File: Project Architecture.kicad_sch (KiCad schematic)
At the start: 0 parts

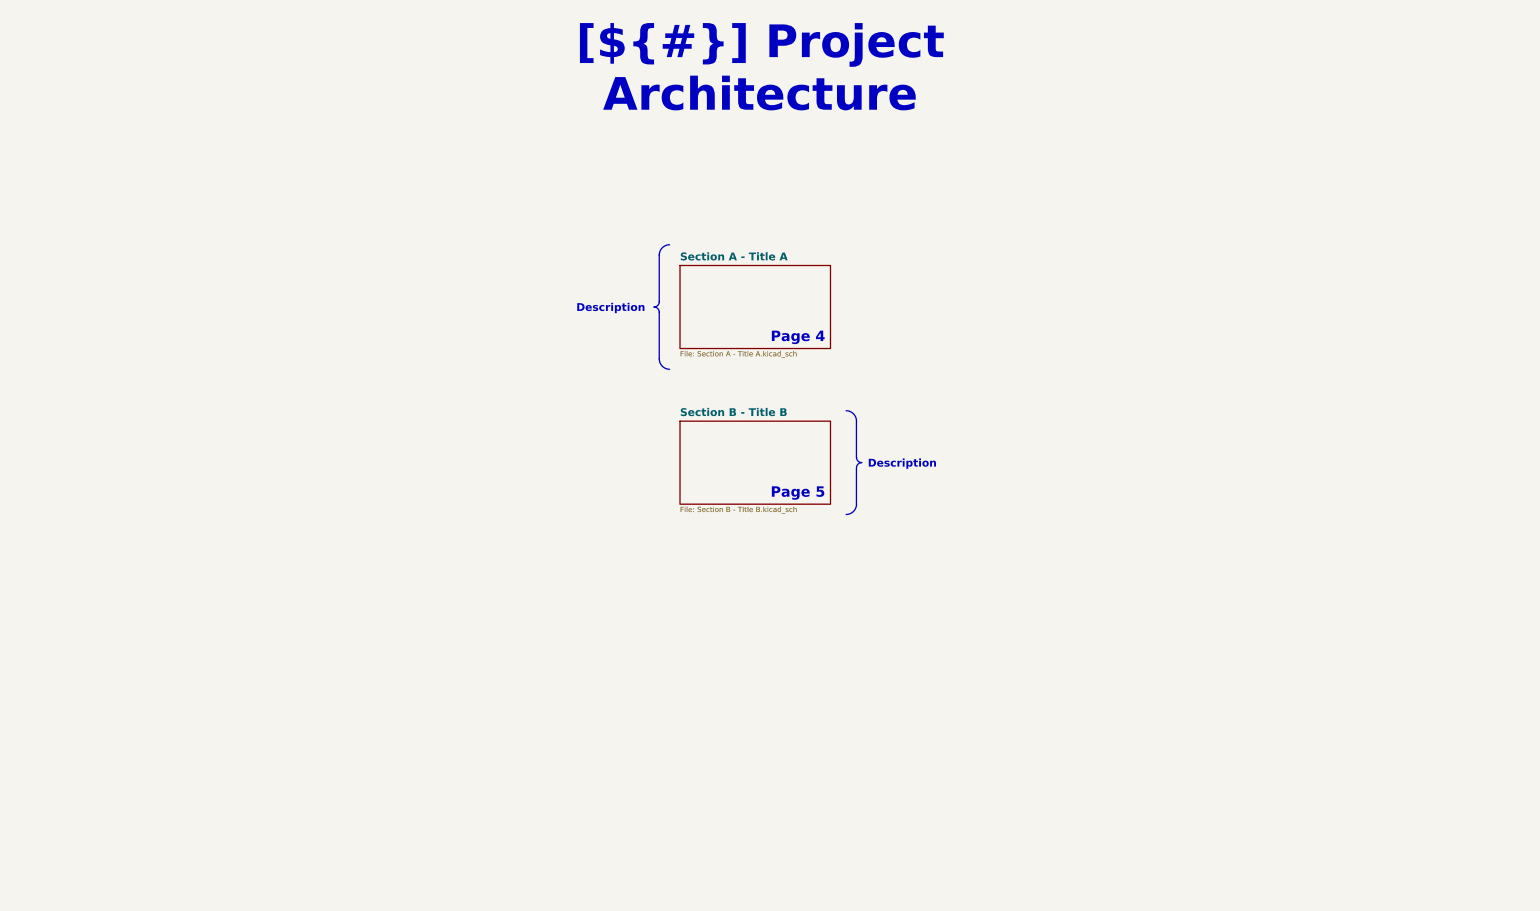
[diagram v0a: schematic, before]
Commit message: Save KiCad 10 design work
Snapshot of the schematic and PCB work done since the initial template
commit: AD7606C-18 ADC, 3x INA241A2 + PBV 1 mOhm shunts, MR60PW phase
connectors, LT8362 boost and LT3045-1 / LTC6655 analog supplies, project
libraries (lib/) and their sym/fp-lib-table.

.gitignore now excludes local history, SpinRender working files, the
stray .step export and Component Search Engine download leftovers.

Co-Authored-By: Claude Opus 5.5 <noreply@anthropic.com>
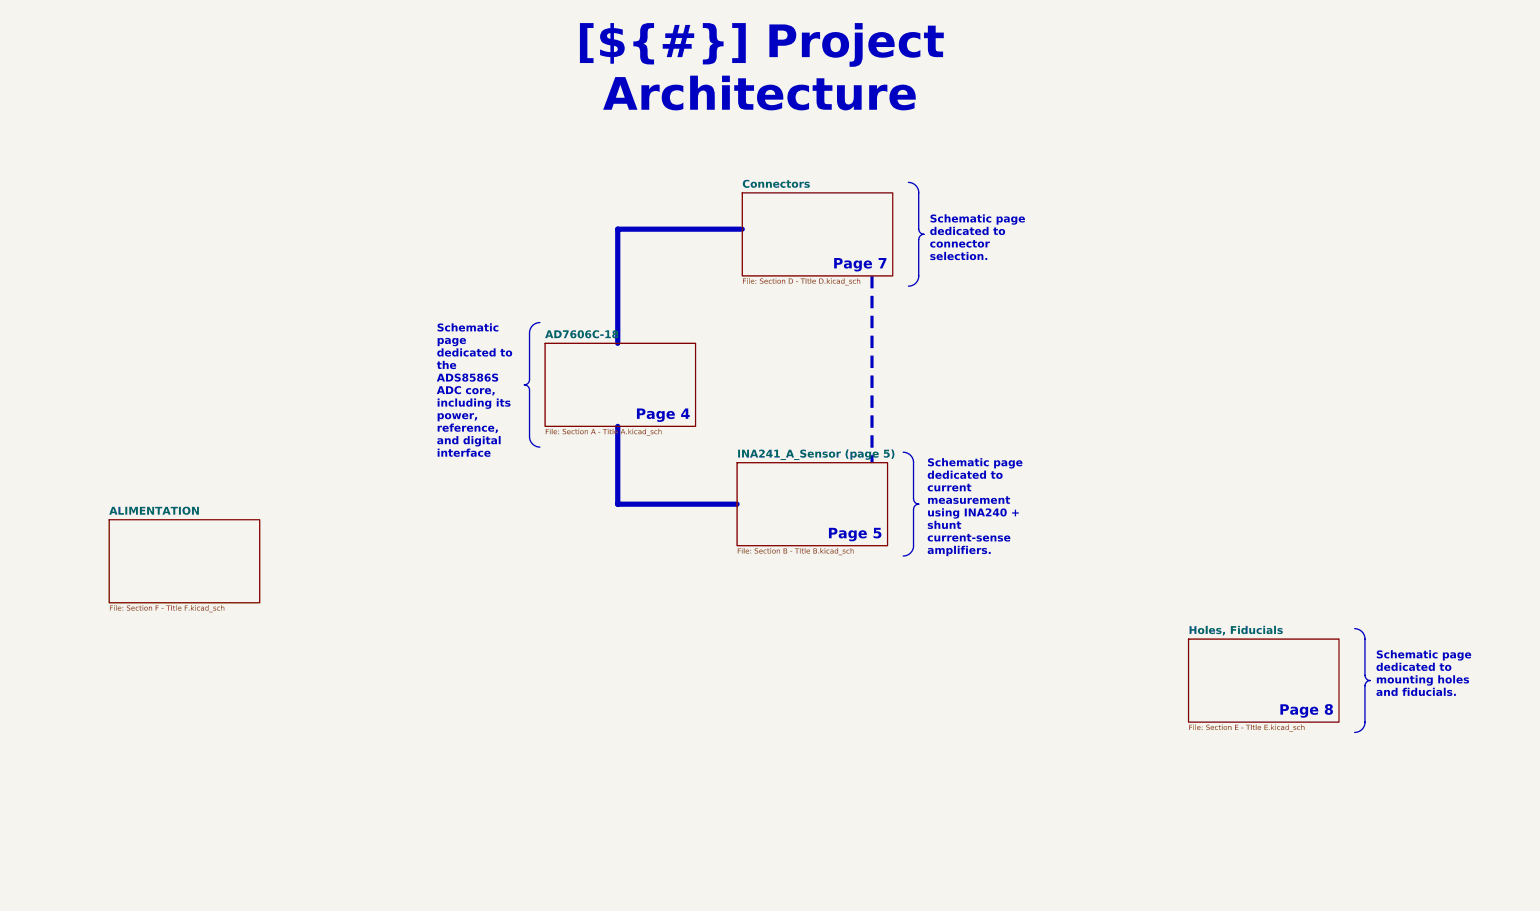
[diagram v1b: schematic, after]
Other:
- sheet Section A - Title A renamed AD7606C-18
- sheet Section B - Title B renamed INA241_A_Sensor (page 5)
- added sheet ALIMENTATION (Section F - TItle F.kicad_sch)
- added sheet Connectors (Section D - TItle D.kicad_sch)
- added sheet Holes, Fiducials (Section E - TItle E.kicad_sch)
- note added: "Page 7"
- note added: "Page 8"

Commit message: Rename to PhaseSense-8586, name sheets by function, self-contained library
Project and sheets
- INA240.* renamed PhaseSense-8586.* (the amplifier is an INA241 and the
  project name was already PhaseSense-8586 in kibot_main.yaml); symbol and
  sheet instances follow the new project name
- "Section X - Title X" sheets renamed after their function: AD7606C-18 -
  ADC, INA241 - Phase Current and Voltage Sense, Connectors, Holes -
  Fiducials, Power Supply - Boost 6V and Analog Rails; hierarchical net
  names updated in the PCB (schematic parity unchanged)
- real titles and dates in the title blocks; Project Architecture and gain
  notes now describe the fitted parts (AD7606C-18, INA241A2 = 20 V/V)

Libraries
- every symbol, footprint and 3D model used by the board is now in
  lib/lib_sym/PhaseSense-8586.kicad_sym, lib/lib_fp/PhaseSense-8586.pretty
  and lib/3d_models, referenced through ${KIPRJMOD}
- removes the footprints without library nickname, the absolute and
  bare-filename 3D paths and the modified-symbol copies (C_1, LT3045_1)

Connectivity is unchanged: the exported netlist is identical before and
after. ERC goes from 62 to 43 violations (footprint links and library
mismatches gone), DRC schematic parity from 33 to 20.

Co-Authored-By: Claude Opus 5.5 <noreply@anthropic.com>
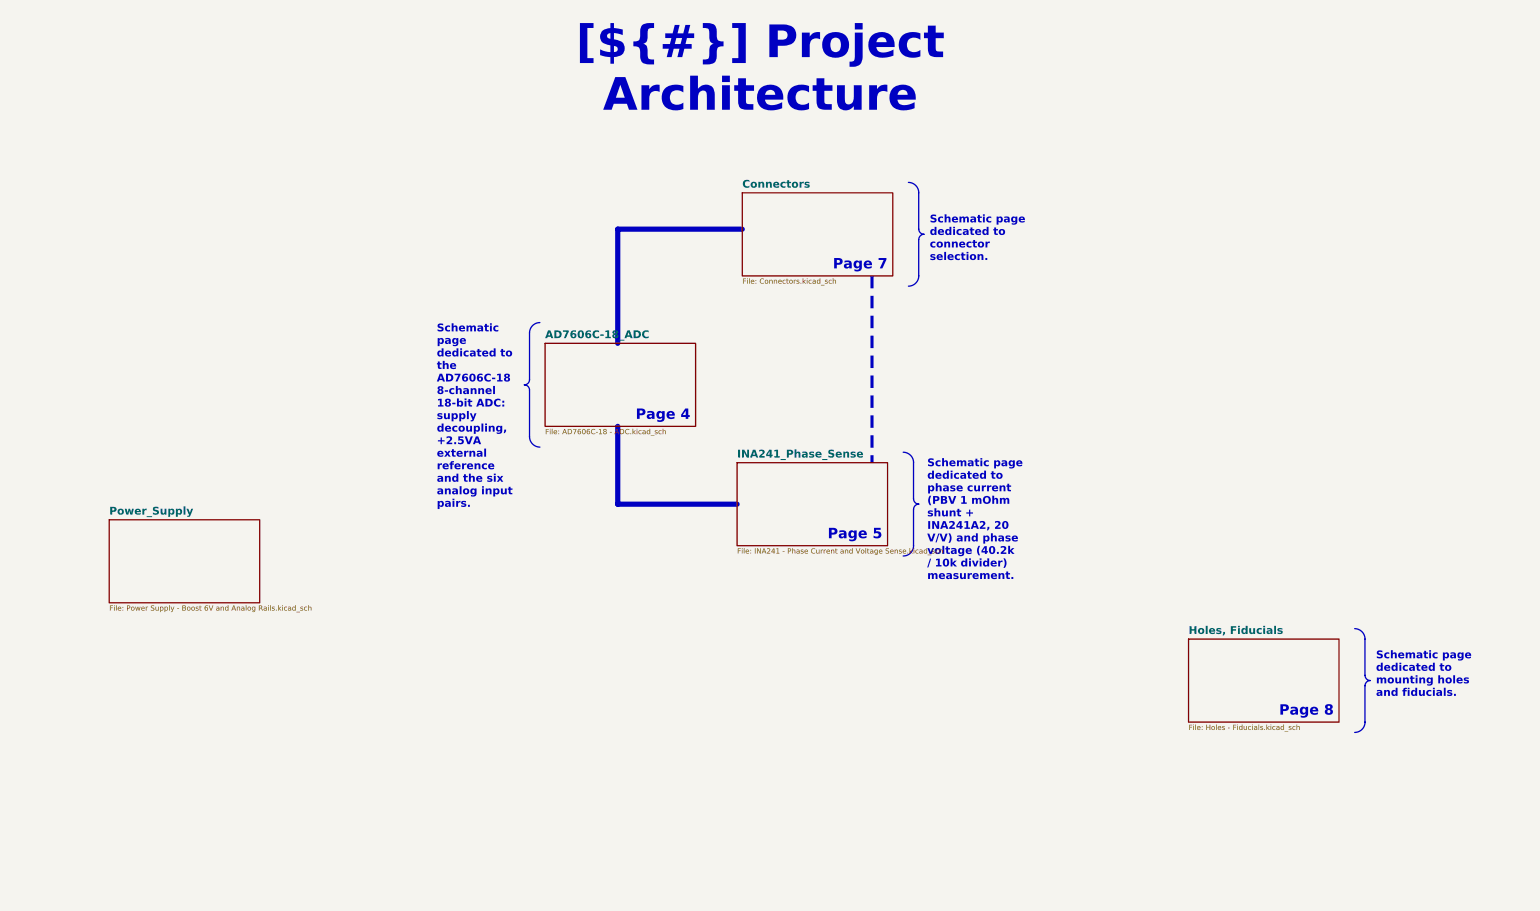
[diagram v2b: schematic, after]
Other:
- sheet AD7606C-18 renamed AD7606C-18_ADC
- sheet ALIMENTATION renamed Power_Supply
- sheet INA241_A_Sensor (page 5) renamed INA241_Phase_Sense
- sheet AD7606C-18_ADC: file Section A - Title A.kicad_sch -> AD7606C-18 - ADC.kicad_sch
- sheet Connectors: file Section D - TItle D.kicad_sch -> Connectors.kicad_sch
- sheet Holes, Fiducials: file Section E - TItle E.kicad_sch -> Holes - Fiducials.kicad_sch
- sheet INA241_Phase_Sense: file Section B - TItle B.kicad_sch -> INA241 - Phase Current and Voltage Sense.kicad_sch
- sheet Power_Supply: file Section F - TItle F.kicad_sch -> Power Supply - Boost 6V and Analog Rails.kicad_sch
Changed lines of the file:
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@@
 	(title_block
 		(title "Project Architecture")
-		(date "2025-01-12")
+		(date "2026-10-05")
 		(rev "${REVISION}")
 		(company "${COMPANY}")
@@
 		)
 	)
-	(text_box "Schematic page dedicated to the ADS8586S ADC core, including its power, reference, and digital interface"
+	(text_box "Schematic page dedicated to the AD7606C-18 8-channel 18-bit ADC: supply decoupling, +2.5VA external reference and the six analog input pairs."
 		(exclude_from_sim no)
 		(at 129.54 88.9 0)
@@
 		)
 	)
-	(text_box "Schematic page dedicated to current measurement using INA240 + shunt current-sense amplifiers."
+	(text_box "Schematic page dedicated to phase current (PBV 1 mOhm shunt + INA241A2, 20 V/V) and phase voltage (40.2k / 10k divider) measurement."
 		(exclude_from_sim no)
 		(at 249.575 121.9 0)
@@
 			(color 255 200 0 0.502)
 		)
-		(property "Sheetname" "ALIMENTATION"
+		(property "Sheetname" "Power_Supply"
 			(at 50.8 137.4009 0)
 			(show_name no)
@@
 			)
 		)
-		(property "Sheetfile" "Section F - TItle F.kicad_sch"
+		(property "Sheetfile" "Power Supply - Boost 6V and Analog Rails.kicad_sch"
 			(at 50.8 159.3346 0)
 			(show_name no)
@@
 		)
 		(instances
-			(project "INA240"
+			(project "PhaseSense-8586"
 				(path "/f9e05184-c88b-4a88-ae9c-ab2bdb32be7c/c5103ceb-5325-4a84-a025-9638a412984e"
 					(page "11")
@@
 			)
 		)
-		(property "Sheetfile" "Section E - TItle E.kicad_sch"
+		(property "Sheetfile" "Holes - Fiducials.kicad_sch"
 			(at 314.96 188.5446 0)
 			(show_name no)
@@
 		)
 		(instances
-			(project "INA240"
+			(project "PhaseSense-8586"
 				(path "/f9e05184-c88b-4a88-ae9c-ab2bdb32be7c/c5103ceb-5325-4a84-a025-9638a412984e"
 					(page "8")
@@
 			)
 		)
-		(property "Sheetfile" "Section D - TItle D.kicad_sch"
+		(property "Sheetfile" "Connectors.kicad_sch"
 			(at 205.74 79.3246 0)
 			(show_name no)
@@
 		)
 		(instances
-			(project "INA240"
+			(project "PhaseSense-8586"
 				(path "/f9e05184-c88b-4a88-ae9c-ab2bdb32be7c/c5103ceb-5325-4a84-a025-9638a412984e"
 					(page "7")
@@
 			(color 255 200 0 0.502)
 		)
-		(property "Sheetname" "INA241_A_Sensor (page 5)"
+		(property "Sheetname" "INA241_Phase_Sense"
 			(at 204.47 123.4309 0)
 			(show_name no)
@@
 			)
 		)
-		(property "Sheetfile" "Section B - TItle B.kicad_sch"
+		(property "Sheetfile" "INA241 - Phase Current and Voltage Sense.kicad_sch"
 			(at 204.47 145.3646 0)
 			(show_name no)
@@
 		)
 		(instances
-			(project "INA240"
+			(project "PhaseSense-8586"
 				(path "/f9e05184-c88b-4a88-ae9c-ab2bdb32be7c/c5103ceb-5325-4a84-a025-9638a412984e"
 					(page "5")
@@
 			(color 128 255 128 0.5)
 		)
-		(property "Sheetname" "AD7606C-18"
+		(property "Sheetname" "AD7606C-18_ADC"
 			(at 157.48 94.2209 0)
 			(show_name no)
@@
 			)
 		)
-		(property "Sheetfile" "Section A - Title A.kicad_sch"
+		(property "Sheetfile" "AD7606C-18 - ADC.kicad_sch"
 			(at 157.48 116.1546 0)
 			(show_name no)
@@
 		)
 		(instances
-			(project "INA240"
+			(project "PhaseSense-8586"
 				(path "/f9e05184-c88b-4a88-ae9c-ab2bdb32be7c/c5103ceb-5325-4a84-a025-9638a412984e"
 					(page "4")

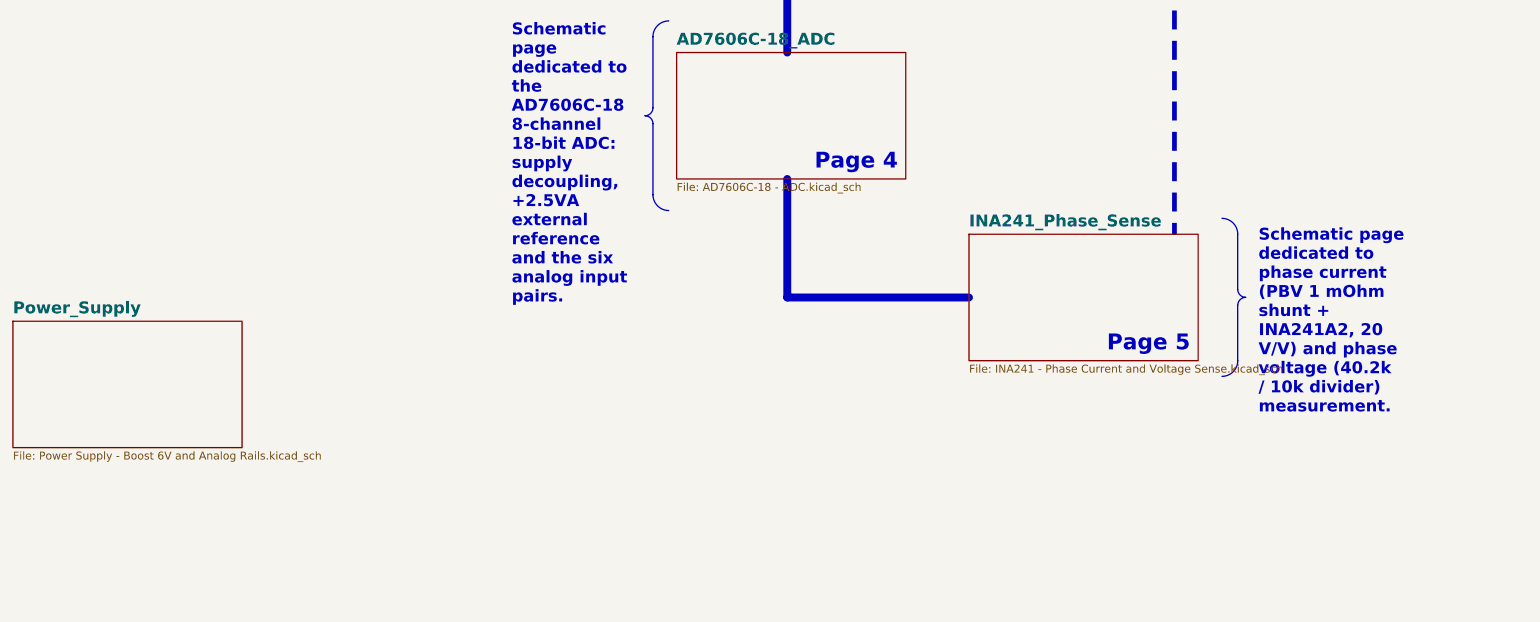
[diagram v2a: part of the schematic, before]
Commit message: Fill template pages: block diagram, power sequencing, cover notes, architecture
- Block Diagram redrawn from the real design: phase path (MR60PW, shunts),
  current and voltage channels with their gains and bandwidths, AD7606C-18,
  power chain, target specifications
- Power - Sequencing: start-up curves taken from the LTspice simulations
  (boost soft-start, analog rails) and rail table with sources, levels
  and timings
- Cover page: real design notes instead of the template examples
- Project Architecture: power-supply block documented, contiguous page
  numbers (Power Supply is page 6)
- Revision History: one column fed by the [Unreleased] changelog section
- sheet titles shortened so they fit the cover-page index: INA241 - Phase
  Sensing, Power Supply - Analog Rails

Sheet-level polylines carry no fill attribute (KiBot schematic reader).

Co-Authored-By: Claude Opus 5.5 <noreply@anthropic.com>
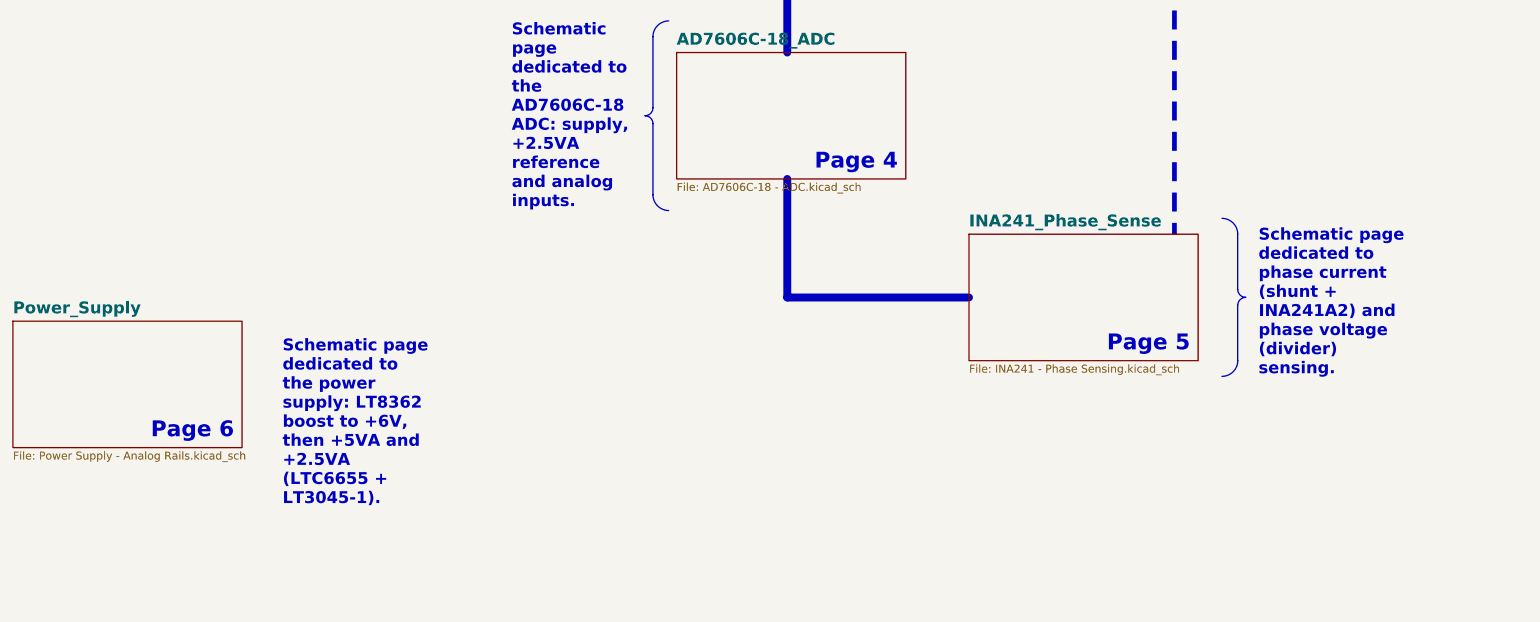
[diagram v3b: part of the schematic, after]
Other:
- sheet INA241_Phase_Sense: file INA241 - Phase Current and Voltage Sense.kicad_sch -> INA241 - Phase Sensing.kicad_sch
- sheet Power_Supply: file Power Supply - Boost 6V and Analog Rails.kicad_sch -> Power Supply - Analog Rails.kicad_sch
- note added: "Page 6"
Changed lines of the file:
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@@
+		)
+	)
+	(text "Page 6"
+		(exclude_from_sim no)
+		(at 86.36 157.48 0)
+		(effects
+			(font
+				(size 2.54 2.54)
+				(bold yes)
+				(color 100 70 50 1)
+			)
+			(justify right bottom)
+			(href "#6")
+		)
+	)
+	(text_box "Schematic page dedicated to the power supply: LT8362 boost to +6V, then +5VA and +2.5VA (LTC6655 + LT3045-1)."
+		(exclude_from_sim no)
+		(at 92.71 139.7 0)
+		(size 26.015 5.1)
+		(margins 1.4287 1.4287 1.4287 1.4287)
+		(stroke
+			(width -0.0001)
+			(type solid)
+		)
+		(fill
+			(type none)
+		)
+		(effects
+			(font
+				(size 1.905 1.905)
+				(thickness 0.381)
+				(bold yes)
+				(color 0 0 0 1)
+			)
+			(justify left top)
 		)
 	)
@@
 		)
 	)
-	(text_box "Schematic page dedicated to the AD7606C-18 8-channel 18-bit ADC: supply decoupling, +2.5VA external reference and the six analog input pairs."
+	(text_box "Schematic page dedicated to the AD7606C-18 ADC: supply, +2.5VA reference and analog inputs."
 		(exclude_from_sim no)
 		(at 129.54 88.9 0)
@@
 		)
 	)
-	(text_box "Schematic page dedicated to phase current (PBV 1 mOhm shunt + INA241A2, 20 V/V) and phase voltage (40.2k / 10k divider) measurement."
+	(text_box "Schematic page dedicated to phase current (shunt + INA241A2) and phase voltage (divider) sensing."
 		(exclude_from_sim no)
 		(at 249.575 121.9 0)
@@
 			)
 		)
-		(property "Sheetfile" "Power Supply - Boost 6V and Analog Rails.kicad_sch"
+		(property "Sheetfile" "Power Supply - Analog Rails.kicad_sch"
 			(at 50.8 159.3346 0)
 			(show_name no)
@@
 			(project "PhaseSense-8586"
 				(path "/f9e05184-c88b-4a88-ae9c-ab2bdb32be7c/c5103ceb-5325-4a84-a025-9638a412984e"
-					(page "11")
+					(page "6")
 				)
 			)
@@
 			)
 		)
-		(property "Sheetfile" "INA241 - Phase Current and Voltage Sense.kicad_sch"
+		(property "Sheetfile" "INA241 - Phase Sensing.kicad_sch"
 			(at 204.47 145.3646 0)
 			(show_name no)
